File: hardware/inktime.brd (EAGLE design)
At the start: 46 x 35 mm, 105 parts, among them IC1 BQ25180YBGR, IC2 DRV2605YZFR, IC3 BMA423, IC9 RT6160AWSC, J1 503480-2400, J2 TC2030-IDC, J4 KH-TYPE-C-16P, Q1 20V/4.2A/52mΩ/1.4W, Q3 SI1308EDL-T1-GE3, U1 NRF52840_QF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

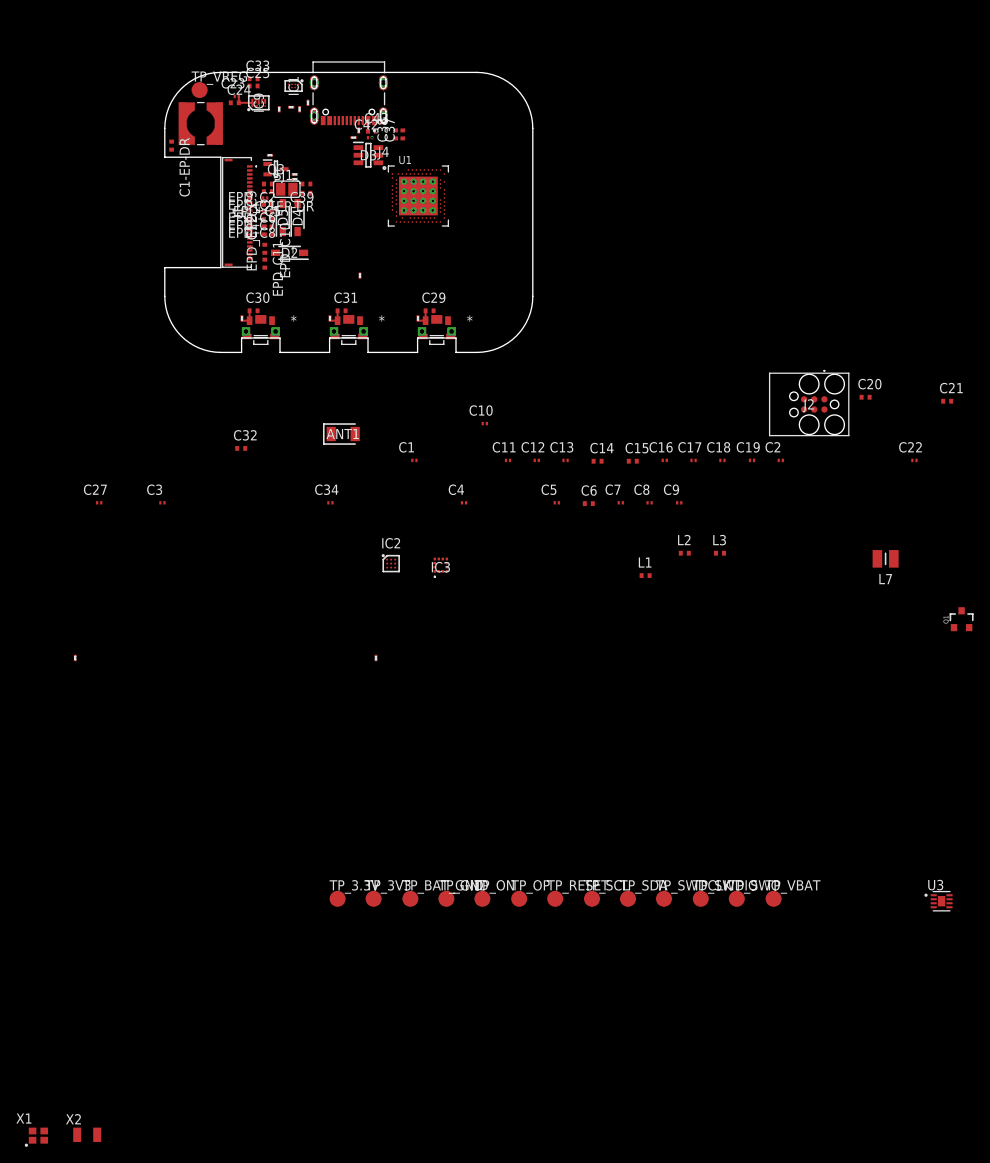
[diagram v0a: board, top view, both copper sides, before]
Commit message: PCB almost done
Signed-off-by: XXMA16 <xxma1610@gmail.com>
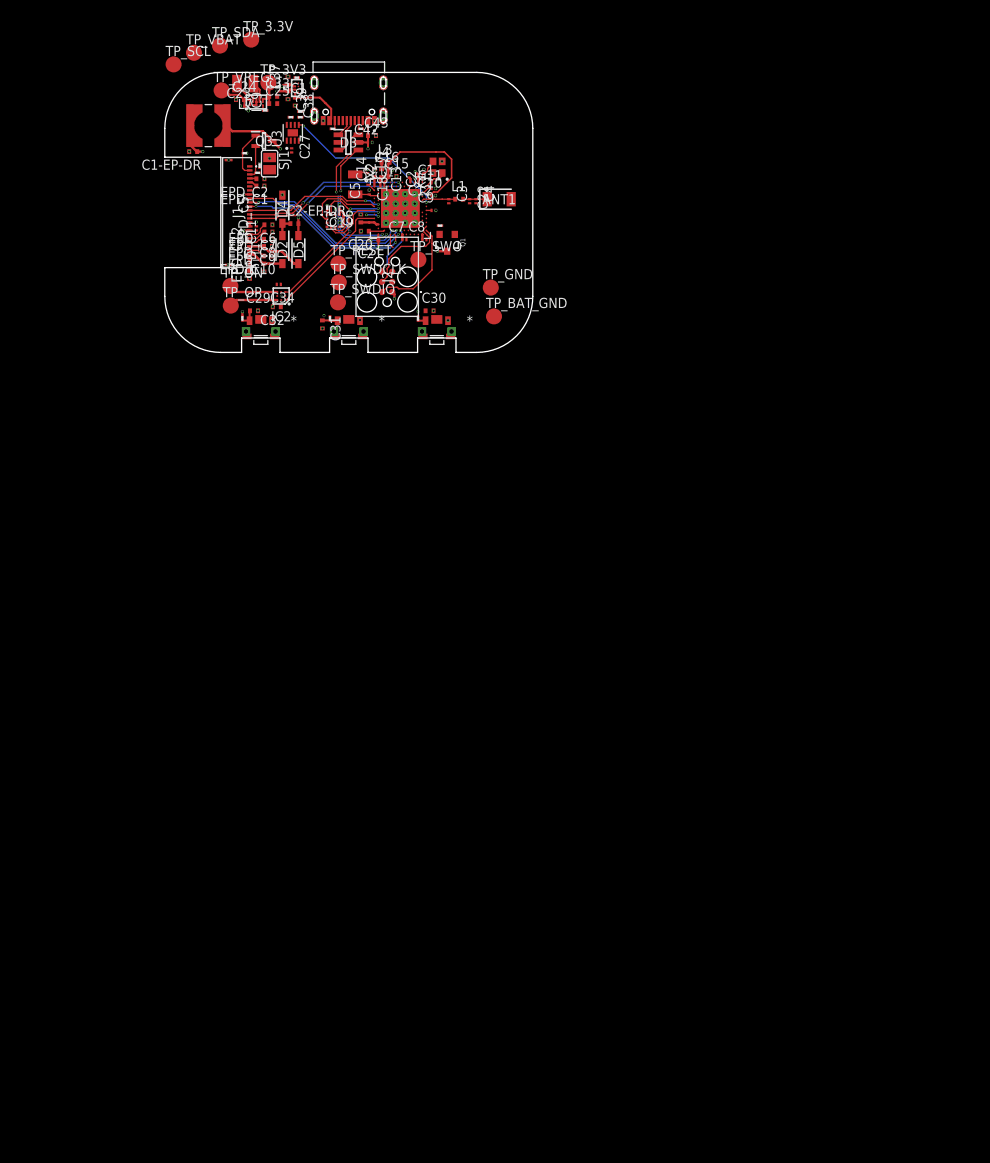
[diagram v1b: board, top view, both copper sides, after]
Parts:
- moved X1 130.9 mm to (11.1, 5.65), turned to 90 degrees
- moved TP_VBAT 128.2 mm to (-19.4, 19.9)
- moved U3 125.7 mm to (-7.00, 9.95), turned to 90 degrees
- moved X2 123.4 mm to (0.80, 3.50), turned to 270 degrees
- moved TP_SDA 118.2 mm to (-16.1, 20.9)
- moved TP_SCL 116.7 mm to (-21.9, 18.5)
- moved TP_3.3V 107.9 mm to (-12.2, 21.6)
- moved TP_3V3 102.8 mm to (-10.1, 16.2)
- moved L7 99.7 mm to (-12.9, 16.1)
- moved TP_SWO 89.3 mm to (8.70, -5.90)
- moved TP_SWDIO 87.3 mm to (-1.35, -11.2)
- moved TP_SWDCLK 87.1 mm to (-1.25, -8.75)
- moved TP_RESET 83.9 mm to (-1.30, -6.40)
- moved TP_ON 82.8 mm to (-14.8, -9.20)
- moved TP_OP 82.4 mm to (-14.8, -11.7)
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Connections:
- removed net D+: D3.4, U1.P$AD6
- removed net D-: D3.6, U1.P$AD4
- new net D_N: D3.4, U1.P$AD4
- new net D_P: D3.6, U1.P$AD6
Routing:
- net EPD_3V3: track 0.00 -> 43.6 mm, vias 0 -> 3
- net 3V3: track 0.40 -> 39.7 mm, vias 0 -> 6
- net VBUS: track 1.32 -> 26.5 mm, vias 0 -> 2
- net SCL: track 0.00 -> 22.2 mm, vias 0 -> 3
- net EPD_BUSY: track 0.00 -> 21.6 mm, vias 0 -> 2
- net EPD_DC: track 0.00 -> 21.5 mm, vias 0 -> 2
- net EPD_RST: track 0.00 -> 21.3 mm, vias 0 -> 2
- net MOSI: track 0.00 -> 20.5 mm, vias 0 -> 2
- net ALERT: track 0.00 -> 20.5 mm, vias 0 -> 2
- net SCK: track 0.00 -> 20.3 mm, vias 0 -> 2
- net N$7: track 0.00 -> 19.7 mm, vias 0 -> 2
- net D_P: track 0.00 -> 19.5 mm, vias 0 -> 2
- net DEC4_6: track 0.00 -> 18.5 mm
- net EPD_CS: track 0.00 -> 17.2 mm, vias 0 -> 2
- net HAPTIC_EN: track 0.00 -> 16.1 mm
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
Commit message: Routing almost done
Signed-off-by: XXMA16 <xxma1610@gmail.com>
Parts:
- moved TP_GND 27.7 mm to (-3.40, 8.45)
- moved TP_BAT_GND 25.3 mm to (5.70, 9.00)
- moved TP_3.3V 24.1 mm to (8.30, 8.95)
- moved TP_VBAT 20.6 mm to (-4.00, 6.20)
- moved TP_SCL 16.2 mm to (-8.35, 9.55)
- moved TP_SDA 12.0 mm to (-8.10, 11.9)
- moved R17 5.15 mm to (-11.2, 11.2), turned to 180 degrees
- moved R4 5.10 mm to (-11.2, 12.5), turned to 0 degrees
- moved R18 2.52 mm to (-9.75, 11.6), turned to 270 degrees
- moved R7 1.98 mm to (-12.2, -11.6), turned to 90 degrees
- moved C27 1.95 mm to (-5.25, 7.30), turned to 0 degrees
- moved U3 1.35 mm to (-5.75, 9.45)
- moved TP_SWO 1.19 mm to (8.25, -4.80)
- moved C29 1.15 mm to (-13.0, -12.4), turned to 180 degrees
- moved TP_RESET 1.02 mm to (-0.30, -6.20)
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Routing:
- net 3V3: track 39.7 -> 114.5 mm, vias 6 -> 15
- net SDA: track 9.43 -> 45.0 mm, vias 1 -> 6
- net P1.02: track 2.15 -> 31.2 mm, vias 0 -> 2
- net SCL: track 22.2 -> 47.3 mm, vias 3 -> 8
- net P0.14: track 8.97 -> 20.2 mm, vias 1 -> 2
- net P0.13: track 2.75 -> 13.9 mm, vias 0 -> 2
- net SWDCLK: track 11.6 -> 19.8 mm, vias 0 -> 2
- net SWDIO: track 12.8 -> 20.5 mm
- net VBAT: track 9.62 -> 16.1 mm, vias 1 -> 2
- net P1.01: track 0.00 -> 5.53 mm, vias 0 -> 2
- net RESET: track 6.23 -> 11.2 mm
- net GND: track 2.98 -> 7.77 mm, vias 56 -> 77
- net P0.00: track 1.69 -> 5.55 mm
- net EPD_3V3: track 43.6 -> 46.3 mm
- net SWO: track 0.00 -> 2.24 mm
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
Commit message: Routing done
Signed-off-by: XXMA16 <xxma1610@gmail.com>
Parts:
- moved TP_BAT_GND 3.18 mm to (6.60, 12.1)
- moved C17 2.55 mm to (2.50, 2.55)
- moved TP_3.3V 1.76 mm to (6.60, 9.40)
- moved ANT1 1.55 mm to (20.4, 1.65)
- moved C3 1.55 mm to (14.1, 1.40)
- moved C22 1.55 mm to (16.6, 1.40)
- moved C4 1.55 mm to (17.4, 1.40)
- moved L1 1.55 mm to (15.3, 1.65)
- moved R2_USB 0.80 mm to (-2.80, 10.4)
- moved C18 0.55 mm to (2.60, 1.45)
- moved TP_GND 0.30 mm to (-3.70, 8.45)
- moved C14 0.25 mm to (3.45, 4.90)
- moved C15 0.25 mm to (5.70, 4.50)
- moved C16 0.25 mm to (5.45, 5.30)
- moved L2 0.25 mm to (4.35, 4.90)
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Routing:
- net PMIC_INT: track 1.56 -> 26.0 mm, vias 2 -> 5
- net VBUS: track 26.2 -> 32.7 mm
- net DP: track 4.61 -> 7.99 mm
- net D_N: track 17.2 -> 20.0 mm
- net 3V3: track 114.5 -> 117.0 mm, vias 15 -> 16
- net DN: track 2.38 -> 4.37 mm
- net N$25: track 4.17 -> 5.72 mm
- net P0.00: track 5.55 -> 4.68 mm
- net GND: track 7.77 -> 8.59 mm, vias 77 -> 80
- net P0.01: track 3.03 -> 3.74 mm
- added copper zone on layer 1, net GND
- added copper zone on layer 16, net GND
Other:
- outline, holes or cut-outs redrawn

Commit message: Minor changes to schematic and PCB
Signed-off-by: XXMA16 <xxma1610@gmail.com>
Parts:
- C15: value 1.0uF -> 1uF
- C23, C27, C34, C42: value 0.1uF -> 100nF
- C43: value 4.7F -> 4.7uF
- moved TP_GND 10.9 mm to (6.60, 12.1)
- moved TP_BAT_GND 10.7 mm to (-3.40, 8.20)
- moved TP_VBAT 0.96 mm to (-3.40, 5.45)
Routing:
- net GND: track 8.59 -> 9.79 mm
- net VBAT: track 16.2 -> 17.1 mm
- net PMIC_INT: vias 5 -> 4
